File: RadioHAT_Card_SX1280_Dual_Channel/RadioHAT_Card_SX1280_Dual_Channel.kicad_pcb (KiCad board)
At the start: 2 copper layers, 30 x 51 mm, 9 parts, among them J2 Conn_Coaxial, J3 Conn_Coaxial

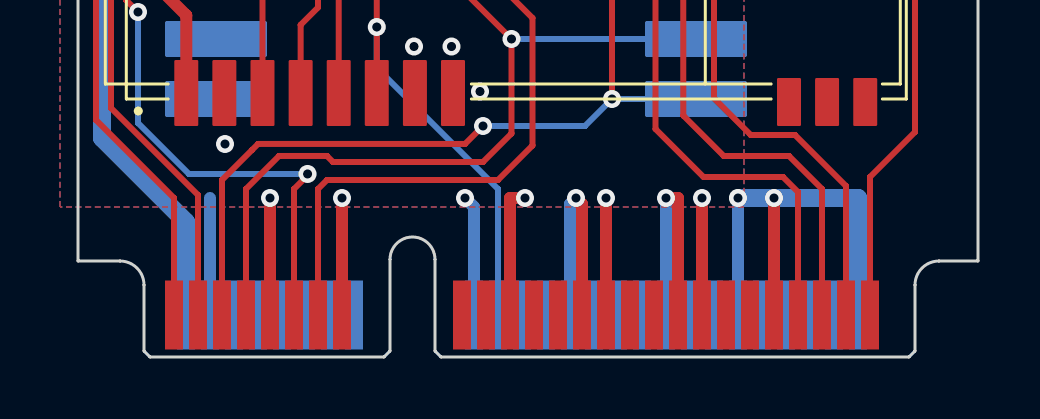
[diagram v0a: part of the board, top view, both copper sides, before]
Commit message: Offset edge connector from board edge to simplify manufacturing
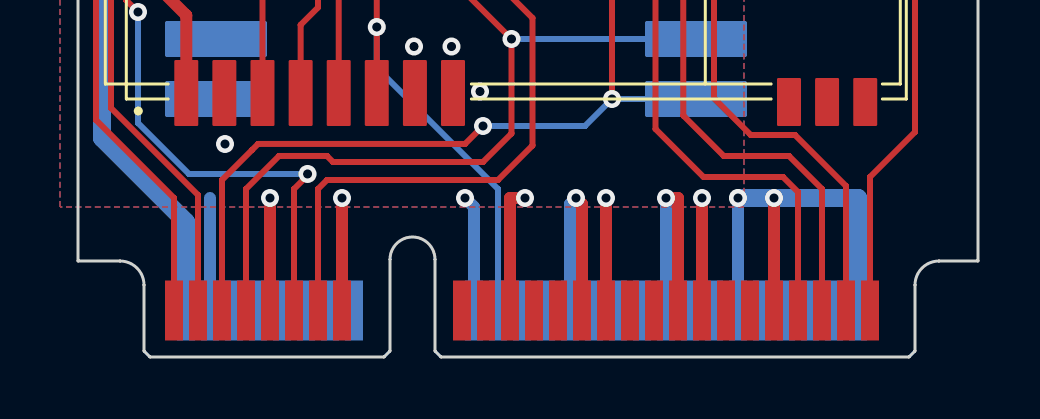
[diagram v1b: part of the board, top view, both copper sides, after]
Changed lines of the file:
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@@
+			)
+		)
+		(fp_text user "${REFERENCE}"
+			(at -8.15 1.75 0)
+			(unlocked yes)
+			(layer "F.Fab")
+			(effects
+				(font
+					(size 1 1)
+					(thickness 0.15)
+				)
 			)
 		)
@@
 		)
 		(pad "1" smd rect
-			(at 1 -1.4 90)
-			(size 2.3 0.6)
+			(at 1 -1.55 90)
+			(size 2 0.6)
 			(layers "F.Cu" "F.Mask" "F.Paste")
 			(net 4 "GPIO0")
@@
 		)
 		(pad "2" smd rect
-			(at 1.4 -1.4 90)
-			(size 2.3 0.6)
+			(at 1.4 -1.55 90)
+			(size 2 0.6)
 			(layers "B.Cu" "B.Mask" "B.Paste")
 			(net 5 "+3V3")
@@
 		)
 		(pad "3" smd rect
-			(at 1.8 -1.4 90)
-			(size 2.3 0.6)
+			(at 1.8 -1.55 90)
+			(size 2 0.6)
 			(layers "F.Cu" "F.Mask" "F.Paste")
 			(net 13 "IRQ0")
@@
 		)
 		(pad "4" smd rect
-			(at 2.2 -1.4 90)
-			(size 2.3 0.6)
+			(at 2.2 -1.55 90)
+			(size 2 0.6)
 			(layers "B.Cu" "B.Mask" "B.Paste")
 			(net 7 "GND")
@@
 		)
 		(pad "5" smd rect
-			(at 2.6 -1.4 90)
-			(size 2.3 0.6)
+			(at 2.6 -1.55 90)
+			(size 2 0.6)
 			(layers "F.Cu" "F.Mask" "F.Paste")
 			(net 6 "IRQ1")
@@
 		)
 		(pad "6" smd rect
-			(at 3 -1.4 90)
-			(size 2.3 0.6)
+			(at 3 -1.55 90)
+			(size 2 0.6)
 			(layers "B.Cu" "B.Mask" "B.Paste")
 			(net 49 "unconnected-(J1-5V-Pad6)")
@@
 		)
 		(pad "7" smd rect
-			(at 3.4 -1.4 90)
-			(size 2.3 0.6)
+			(at 3.4 -1.55 90)
+			(size 2 0.6)
 			(layers "F.Cu" "F.Mask" "F.Paste")
 			(net 16 "GPIO1")
@@
 		)
 		(pad "8" smd rect
-			(at 3.8 -1.4 90)
-			(size 2.3 0.6)
+			(at 3.8 -1.55 90)
+			(size 2 0.6)
 			(layers "B.Cu" "B.Mask" "B.Paste")
 			(thermal_bridge_angle 0)
 		)
 		(pad "9" smd rect
-			(at 4.2 -1.4 90)
-			(size 2.3 0.6)
+			(at 4.2 -1.55 90)
+			(size 2 0.6)
 			(layers "F.Cu" "F.Mask" "F.Paste")
 			(net 7 "GND")
@@
 		)
 		(pad "10" smd rect
-			(at 4.6 -1.4 90)
-			(size 2.3 0.6)
+			(at 4.6 -1.55 90)
+			(size 2 0.6)
 			(layers "B.Cu" "B.Mask" "B.Paste")
 			(thermal_bridge_angle 0)
 		)
 		(pad "11" smd rect
-			(at 5 -1.4 90)
-			(size 2.3 0.6)
+			(at 5 -1.55 90)
+			(size 2 0.6)
 			(layers "F.Cu" "F.Mask" "F.Paste")
 			(net 2 "RST0")
@@
 		)
 		(pad "12" smd rect
-			(at 5.4 -1.4 90)
-			(size 2.3 0.6)
+			(at 5.4 -1.55 90)
+			(size 2 0.6)
 			(layers "B.Cu" "B.Mask" "B.Paste")
 			(thermal_bridge_angle 0)
 		)
 		(pad "13" smd rect
-			(at 5.8 -1.4 90)
-			(size 2.3 0.6)
+			(at 5.8 -1.55 90)
+			(size 2 0.6)
 			(layers "F.Cu" "F.Mask" "F.Paste")
 			(net 12 "RST1")
@@
 		)
 		(pad "14" smd rect
-			(at 6.2 -1.4 90)
-			(size 2.3 0.6)
+			(at 6.2 -1.55 90)
+			(size 2 0.6)
 			(layers "B.Cu" "B.Mask" "B.Paste")
 			(thermal_bridge_angle 0)
 		)
 		(pad "15" smd rect
-			(at 6.6 -1.4 90)
-			(size 2.3 0.6)
+			(at 6.6 -1.55 90)
+			(size 2 0.6)
 			(layers "F.Cu" "F.Mask" "F.Paste")
 			(net 7 "GND")
@@
 		)
 		(pad "16" smd rect
-			(at 7 -1.4 90)
-			(size 2.3 0.6)
+			(at 7 -1.55 90)
+			(size 2 0.6)
 			(layers "B.Cu" "B.Mask" "B.Paste")
 			(thermal_bridge_angle 0)
 		)
 		(pad "17" smd rect
-			(at 10.6 -1.4 90)
-			(size 2.3 0.6)
+			(at 10.6 -1.55 90)
+			(size 2 0.6)
 			(layers "F.Cu" "F.Mask" "F.Paste")
 			(thermal_bridge_angle 0)
 		)
 		(pad "18" smd rect
-			(at 11 -1.4 90)
-			(size 2.3 0.6)
+			(at 11 -1.55 90)
+			(size 2 0.6)
 			(layers "B.Cu" "B.Mask" "B.Paste")
 			(net 7 "GND")
@@
 		)
 		(pad "19" smd rect
-			(at 11.4 -1.4 90)
-			(size 2.3 0.6)
+			(at 11.4 -1.55 90)
+			(size 2 0.6)
 			(layers "F.Cu" "F.Mask" "F.Paste")
 			(thermal_bridge_angle 0)
 		)
 		(pad "20" smd rect
-			(at 11.8 -1.4 90)
-			(size 2.3 0.6)
+			(at 11.8 -1.55 90)
+			(size 2 0.6)
 			(layers "B.Cu" "B.Mask" "B.Paste")
 			(net 17 "NSS1")
@@
 		)
 		(pad "21" smd rect
-			(at 12.2 -1.4 90)
-			(size 2.3 0.6)
+			(at 12.2 -1.55 90)
+			(size 2 0.6)
 			(layers "F.Cu" "F.Mask" "F.Paste")
 			(net 7 "GND")
@@
 		)
 		(pad "22" smd rect
-			(at 12.6 -1.4 90)
-			(size 2.3 0.6)
+			(at 12.6 -1.55 90)
+			(size 2 0.6)
 			(layers "B.Cu" "B.Mask" "B.Paste")
 			(thermal_bridge_angle 0)
 		)
 		(pad "23" smd rect
-			(at 13 -1.4 90)
-			(size 2.3 0.6)
+			(at 13 -1.55 90)
+			(size 2 0.6)
 			(layers "F.Cu" "F.Mask" "F.Paste")
 			(thermal_bridge_angle 0)
 		)
 		(pad "24" smd rect
-			(at 13.4 -1.4 90)
-			(size 2.3 0.6)
+			(at 13.4 -1.55 90)
+			(size 2 0.6)
 			(layers "B.Cu" "B.Mask" "B.Paste")
 			(net 48 "unconnected-(J1-3V3-Pad24)")
@@
 		)
 		(pad "25" smd rect
-			(at 13.8 -1.4 90)
-			(size 2.3 0.6)
+			(at 13.8 -1.55 90)
+			(size 2 0.6)
 			(layers "F.Cu" "F.Mask" "F.Paste")
 			(thermal_bridge_angle 0)
 		)
 		(pad "26" smd rect
-			(at 14.2 -1.4 90)
-			(size 2.3 0.6)
+			(at 14.2 -1.55 90)
+			(size 2 0.6)
 			(layers "B.Cu" "B.Mask" "B.Paste")
 			(net 7 "GND")
@@
 		)
 		(pad "27" smd rect
-			(at 14.6 -1.4 90)
-			(size 2.3 0.6)
+			(at 14.6 -1.55 90)
+			(size 2 0.6)
 			(layers "F.Cu" "F.Mask" "F.Paste")
 			(net 7 "GND")
@@
 		)
 		(pad "28" smd rect
-			(at 15 -1.4 90)
-			(size 2.3 0.6)
+			(at 15 -1.55 90)
+			(size 2 0.6)
 			(layers "B.Cu" "B.Mask" "B.Paste")
 			(net 50 "unconnected-(J1-5V-Pad28)")
@@
 		)
 		(pad "29" smd rect
-			(at 15.4 -1.4 90)
-			(size 2.3 0.6)
+			(at 15.4 -1.55 90)
+			(size 2 0.6)
 			(layers "F.Cu" "F.Mask" "F.Paste")
 			(net 7 "GND")
@@
 		)
 		(pad "30" smd rect
-			(at 15.8 -1.4 90)
-			(size 2.3 0.6)
+			(at 15.8 -1.55 90)
+			(size 2 0.6)
 			(layers "B.Cu" "B.Mask" "B.Paste")
 			(net 8 "unconnected-(J1-I2C_SCL-Pad30)")
@@
 		)
 		(pad "31" smd rect
-			(at 16.2 -1.4 90)
-			(size 2.3 0.6)
+			(at 16.2 -1.55 90)
+			(size 2 0.6)
 			(layers "F.Cu" "F.Mask" "F.Paste")
 			(net 11 "unconnected-(J1-PPS-Pad31)")
@@
 		)
 		(pad "32" smd rect
-			(at 16.6 -1.4 90)
-			(size 2.3 0.6)
+			(at 16.6 -1.55 90)
+			(size 2 0.6)
 			(layers "B.Cu" "B.Mask" "B.Paste")
 			(net 14 "unconnected-(J1-I2C_SCL-Pad32)")
@@
 		)
 		(pad "33" smd rect
-			(at 17 -1.4 90)
-			(size 2.3 0.6)
+			(at 17 -1.55 90)
+			(size 2 0.6)
 			(layers "F.Cu" "F.Mask" "F.Paste")
 			(thermal_bridge_angle 0)
 		)
 		(pad "34" smd rect
-			(at 17.4 -1.4 90)
-			(size 2.3 0.6)
+			(at 17.4 -1.55 90)
+			(size 2 0.6)
 			(layers "B.Cu" "B.Mask" "B.Paste")
 			(net 7 "GND")
@@
 		)
 		(pad "35" smd rect
-			(at 17.8 -1.4 90)
-			(size 2.3 0.6)
+			(at 17.8 -1.55 90)
+			(size 2 0.6)
 			(layers "F.Cu" "F.Mask" "F.Paste")
 			(net 7 "GND")
@@
 		)
 		(pad "36" smd rect
-			(at 18.2 -1.4 90)
-			(size 2.3 0.6)
+			(at 18.2 -1.55 90)
+			(size 2 0.6)
 			(layers "B.Cu" "B.Mask" "B.Paste")
 			(net 15 "unconnected-(J1-USB_D--Pad36)")
@@
 		)
 		(pad "37" smd rect
-			(at 18.6 -1.4 90)
-			(size 2.3 0.6)
+			(at 18.6 -1.55 90)
+			(size 2 0.6)
 			(layers "F.Cu" "F.Mask" "F.Paste")
 			(net 7 "GND")
@@
 		)
 		(pad "38" smd rect
-			(at 19 -1.4 90)
-			(size 2.3 0.6)
+			(at 19 -1.55 90)
+			(size 2 0.6)
 			(layers "B.Cu" "B.Mask" "B.Paste")
 			(net 21 "unconnected-(J1-USB_D+-Pad38)")
@@
 		)
 		(pad "39" smd rect
-			(at 19.4 -1.4 90)
-			(size 2.3 0.6)
+			(at 19.4 -1.55 90)
+			(size 2 0.6)
 			(layers "F.Cu" "F.Mask" "F.Paste")
 			(net 52 "unconnected-(J1-3V3-Pad39)")
@@
 		)
 		(pad "40" smd rect
-			(at 19.8 -1.4 90)
-			(size 2.3 0.6)
+			(at 19.8 -1.55 90)
+			(size 2 0.6)
 			(layers "B.Cu" "B.Mask" "B.Paste")
 			(net 7 "GND")
@@
 		)
 		(pad "41" smd rect
-			(at 20.2 -1.4 90)
-			(size 2.3 0.6)
+			(at 20.2 -1.55 90)
+			(size 2 0.6)
 			(layers "F.Cu" "F.Mask" "F.Paste")
 			(net 53 "unconnected-(J1-3V3-Pad41)")
@@
 		)
 		(pad "42" smd rect
-			(at 20.6 -1.4 90)
-			(size 2.3 0.6)
+			(at 20.6 -1.55 90)
+			(size 2 0.6)
 			(layers "B.Cu" "B.Mask" "B.Paste")
 			(net 19 "unconnected-(J1-LED0-Pad42)")
@@
 		)
 		(pad "43" smd rect
-			(at 21 -1.4 90)
-			(size 2.3 0.6)
+			(at 21 -1.55 90)
+			(size 2 0.6)
 			(layers "F.Cu" "F.Mask" "F.Paste")
 			(net 7 "GND")
@@
 		)
 		(pad "44" smd rect
-			(at 21.4 -1.4 90)
-			(size 2.3 0.6)
+			(at 21.4 -1.55 90)
+			(size 2 0.6)
 			(layers "B.Cu" "B.Mask" "B.Paste")
 			(net 18 "unconnected-(J1-LED1-Pad44)")
@@
 		)
 		(pad "45" smd rect
-			(at 21.8 -1.4 90)
-			(size 2.3 0.6)
+			(at 21.8 -1.55 90)
+			(size 2 0.6)
 			(layers "F.Cu" "F.Mask" "F.Paste")
 			(net 9 "SCK")
@@
 		)
 		(pad "46" smd rect
-			(at 22.2 -1.4 90)
-			(size 2.3 0.6)
+			(at 22.2 -1.55 90)
+			(size 2 0.6)
 			(layers "B.Cu" "B.Mask" "B.Paste")
 			(net 20 "unconnected-(J1-LED2-Pad46)")
@@
 		)
 		(pad "47" smd rect
-			(at 22.6 -1.4 90)
-			(size 2.3 0.6)
+			(at 22.6 -1.55 90)
+			(size 2 0.6)
 			(layers "F.Cu" "F.Mask" "F.Paste")
 			(net 1 "MISO")
@@
 		)
 		(pad "48" smd rect
-			(at 23 -1.4 90)
-			(size 2.3 0.6)
+			(at 23 -1.55 90)
+			(size 2 0.6)
 			(layers "B.Cu" "B.Mask" "B.Paste")
 			(net 51 "unconnected-(J1-5V-Pad48)")
@@
 		)
 		(pad "49" smd rect
-			(at 23.4 -1.4 90)
-			(size 2.3 0.6)
+			(at 23.4 -1.55 90)
+			(size 2 0.6)
 			(layers "F.Cu" "F.Mask" "F.Paste")
 			(net 10 "MOSI")
@@
 		)
 		(pad "50" smd rect
-			(at 23.8 -1.4 90)
-			(size 2.3 0.6)
+			(at 23.8 -1.55 90)
+			(size 2 0.6)
 			(layers "B.Cu" "B.Mask" "B.Paste")
 			(net 7 "GND")
@@
 		)
 		(pad "51" smd rect
-			(at 24.2 -1.4 90)
-			(size 2.3 0.6)
+			(at 24.2 -1.55 90)
+			(size 2 0.6)
 			(layers "F.Cu" "F.Mask" "F.Paste")
 			(net 3 "NSS0")
